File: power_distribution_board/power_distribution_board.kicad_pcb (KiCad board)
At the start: 2 copper layers, 67 parts, among them J1 CONN_01x03, J10 CONN_02X01, J11 CONN_02X01, J12 CONN_02X01, J13 CONN_02X01, J14 CONN_02X01, J15 CONN_02X01, J16 CONN_02X01, J17 CONN_02X01, J18 CONN_02X01, J19 CONN_02X01, J2 CONN_02X01, J20 CONN_02X01, J21 CONN_02X01, J22 CONN_02X01, J23 CONN_02X01, J3 CONN_02X01, J4 CONN_02X01, J5 CONN_02X01, J6 CONN_02X01, J7 CONN_02X01, J8 CONN_02X01, J9 CONN_02X01, Q1 NMOS_SSSGD, Q2 NMOS_SSSGD, Q3 NMOS_SSSGD, Q4 NMOS_SSSGD, Q5 Q_NMOS_GSD, U1 EHHD015A0A, U2 LTC1473, U3 EHHD010A0B, U4 LM317EMP, U5 BTS6133D, U6 A1120

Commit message: initial attempt at routing for LTC1743
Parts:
- moved J23 213.1 mm to (31.5, 116.5)
- moved J22 211.4 mm to (24.5, 116.5)
- moved D3 48.2 mm to (44.2, 131.2), turned to 180 degrees
- moved D5 37.2 mm to (44.2, 135.8), turned to 180 degrees
- moved Q3 33.4 mm to (62.8, 147.8), turned to 270 degrees
- moved R9 31.8 mm to (78.8, 138.0), turned to 180 degrees
- moved D6 25.4 mm to (46.0, 142.5), turned to 270 degrees
- moved Q2 22.7 mm to (71.0, 129.5), turned to 90 degrees
- moved Q4 21.5 mm to (69.2, 147.8), turned to 270 degrees
- moved Q1 17.4 mm to (64.5, 129.5), turned to 90 degrees
- moved C1 13.6 mm to (52.0, 140.0), turned to 270 degrees
- moved J1 13.6 mm to (57.8, 127.2), turned to 180 degrees
- moved C3 13.1 mm to (55.0, 140.0), turned to 270 degrees
- moved C2 12.3 mm to (53.5, 140.0), turned to 270 degrees
- moved R7 11.8 mm to (52.2, 137.0), turned to 180 degrees
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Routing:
- net Net-(R9-Pad2): track 0.00 -> 21.2 mm
- net Net-(R9-Pad3): track 0.00 -> 15.4 mm
- net Net-(Q2-Pad4): track 0.00 -> 13.7 mm
- net Net-(L1-Pad2): track 0.00 -> 12.6 mm
- net Net-(R5-Pad2): track 0.00 -> 8.75 mm
- net Net-(Q4-Pad4): track 0.00 -> 7.74 mm
- net Net-(Q3-Pad4): track 0.00 -> 6.91 mm
- net Net-(Q1-Pad4): track 0.00 -> 6.79 mm
- net Net-(C1-Pad1): track 0.00 -> 5.81 mm
- net Net-(J1-Pad1): track 0.00 -> 5.46 mm
- net Net-(J1-Pad3): track 0.00 -> 5.34 mm
- net Net-(J1-Pad2): track 0.00 -> 5.02 mm
- net Net-(R6-Pad2): track 0.00 -> 4.44 mm
- net Net-(C2-Pad1): track 0.00 -> 4.25 mm
- net Net-(R8-Pad2): track 0.00 -> 2.49 mm
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
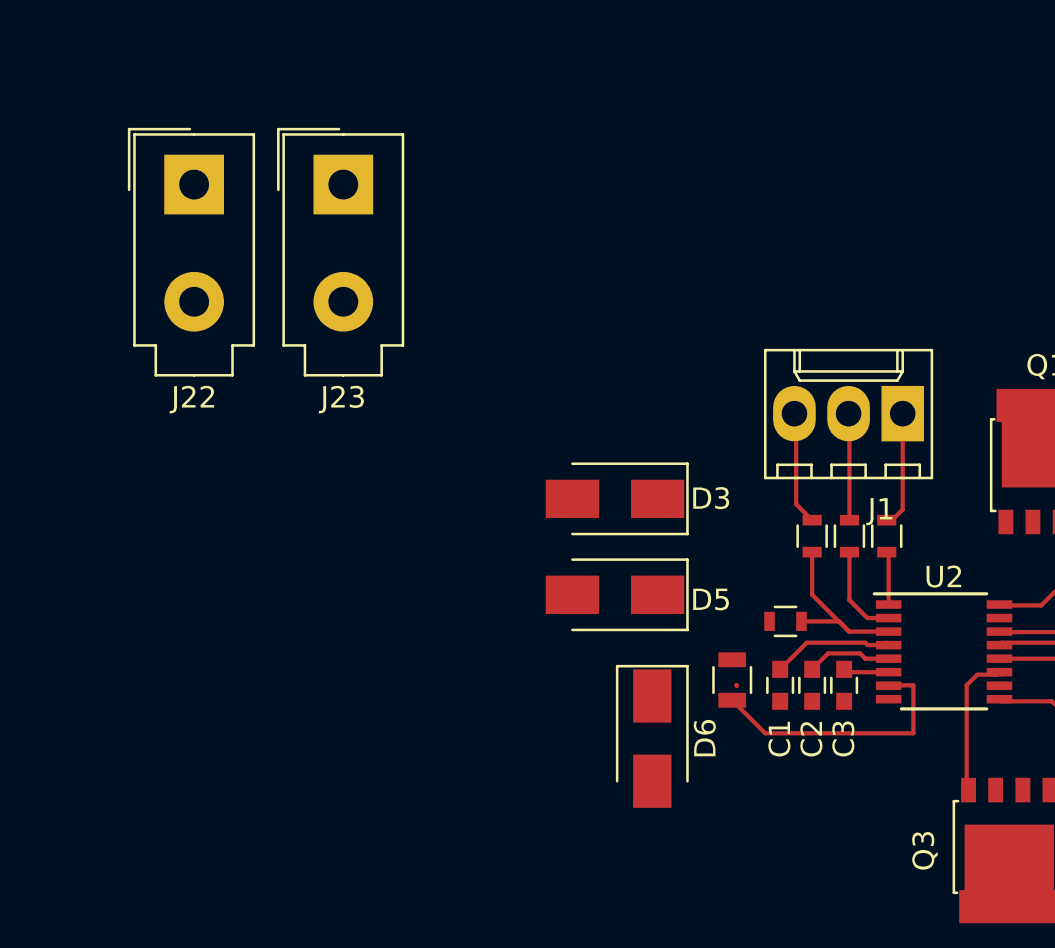
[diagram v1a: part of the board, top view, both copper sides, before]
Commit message: minor improvements to LTC1473 routing
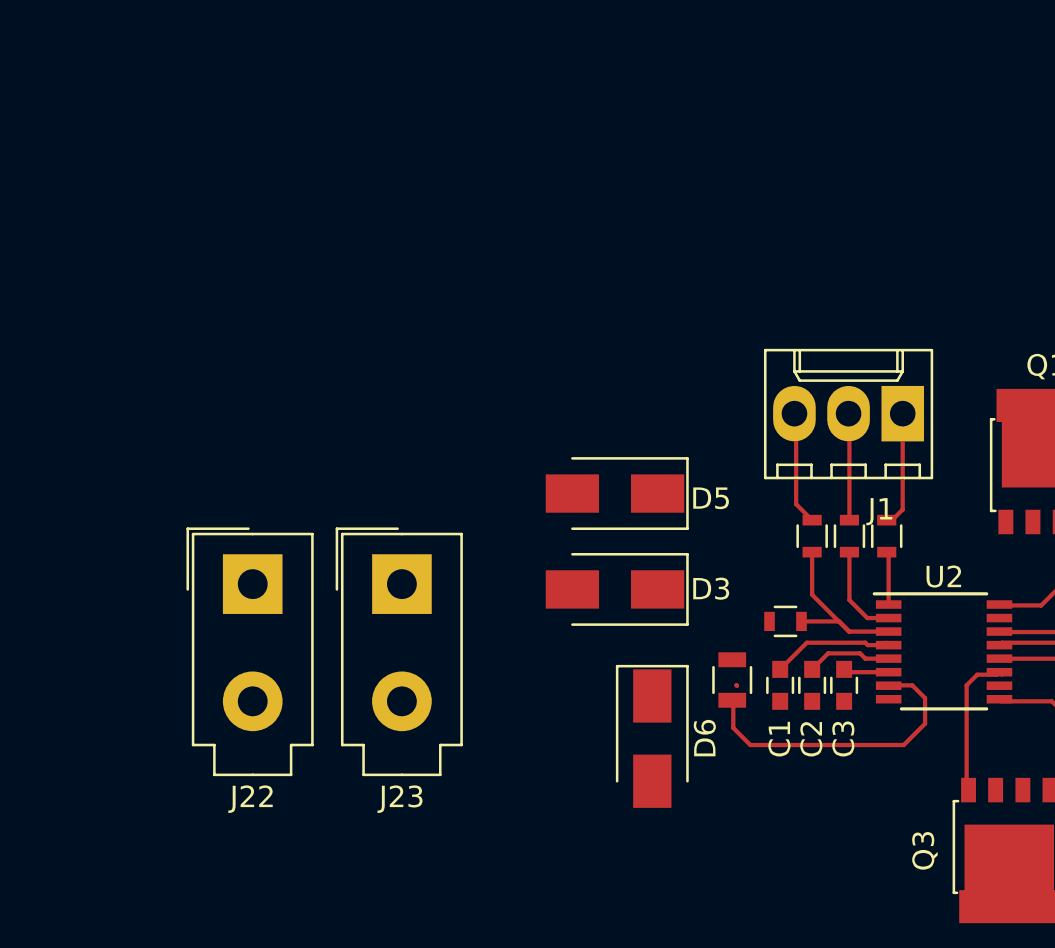
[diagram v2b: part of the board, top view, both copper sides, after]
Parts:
- moved J22 19.0 mm to (27.2, 135.2)
- moved J23 19.0 mm to (34.2, 135.2)
- moved D5 4.75 mm to (44.2, 131.0)
- moved D3 4.25 mm to (44.2, 135.5)
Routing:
- net Net-(L1-Pad2): track 12.6 -> 14.3 mm
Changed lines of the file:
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@@
     (thickness 1.6)
     (drawings 0)
-    (tracks 69)
+    (tracks 74)
     (zones 0)
     (modules 67)
@@
   )
   (module Diodes_SMD:D_SMA (layer F.Cu)
-    (at 44.25 131.25 180)
+    (at 44.25 135.5 180)
     (descr "Diode SMA (DO-214AC)")
     (tags "Diode SMA (DO-214AC)")
@@
   )
   (module Diodes_SMD:D_SMA (layer F.Cu)
-    (at 44.25 135.75 180)
+    (at 44.25 131 180)
     (descr "Diode SMA (DO-214AC)")
     (tags "Diode SMA (DO-214AC)")
@@
   )
   (module Connectors_Molex:Molex_MiniFit-JR-5556-02A_2x01x4.20mm_Straight (layer F.Cu)
-    (at 24.5 116.5)
+    (at 27.25 135.25)
     (descr "Molex Mini-Fit JR, PN:5556-02A, dual row, top entry type, through hole")
     (tags "connector molex mini-fit 5556")
@@
   )
   (module Connectors_Molex:Molex_MiniFit-JR-5556-02A_2x01x4.20mm_Straight (layer F.Cu)
-    (at 31.5 116.5)
+    (at 34.25 135.25)
     (descr "Molex Mini-Fit JR, PN:5556-02A, dual row, top entry type, through hole")
     (tags "connector molex mini-fit 5556")
@@
   (segment (start 52.75 131.5) (end 52.75 127.33) (width 0.2) (layer F.Cu) (net 15) (status 20))
   (segment (start 52.75 127.33) (end 52.67 127.25) (width 0.2) (layer F.Cu) (net 15) (status 30))
-  (segment (start 57.09 140.0175) (end 57.1075 140) (width 0.2) (layer F.Cu) (net 19))
-  (segment (start 57.1075 140) (end 58.25 140) (width 0.2) (layer F.Cu) (net 19))
-  (segment (start 58.25 140) (end 58.25 142.25) (width 0.2) (layer F.Cu) (net 19))
-  (segment (start 58.25 142.25) (end 51.3 142.25) (width 0.2) (layer F.Cu) (net 19))
-  (segment (start 51.3 142.25) (end 49.75 140.7) (width 0.2) (layer F.Cu) (net 19))
+  (segment (start 57.09 140.0175) (end 57.1075 140) (width 0.2) (layer F.Cu) (net 19) (status C00000))
+  (segment (start 57.1075 140) (end 58.2 140) (width 0.2) (layer F.Cu) (net 19) (status 400000))
+  (segment (start 49.8 142) (end 49.8 140.75) (width 0.2) (layer F.Cu) (net 19) (status 800000))
+  (segment (start 50.6 142.8) (end 49.8 142) (width 0.2) (layer F.Cu) (net 19))
+  (segment (start 57.8 142.8) (end 50.6 142.8) (width 0.2) (layer F.Cu) (net 19))
+  (segment (start 58.8 141.8) (end 57.8 142.8) (width 0.2) (layer F.Cu) (net 19))
+  (segment (start 58.8 140.6) (end 58.8 141.8) (width 0.2) (layer F.Cu) (net 19))
+  (segment (start 58.2 140) (end 58.8 140.6) (width 0.2) (layer F.Cu) (net 19))
+  (segment (start 49.8 140.75) (end 49.75 140.7) (width 0.2) (layer F.Cu) (net 19) (status C00000))
+  (segment (start 49.8 140.75) (end 49.75 140.7) (width 0.2) (layer F.Cu) (net 19) (status C00000))
   (segment (start 66.41 132.335) (end 66.25 132.495) (width 0.2) (layer F.Cu) (net 21) (status 30))
   (segment (start 66.25 132.495) (end 66.25 134.25) (width 0.2) (layer F.Cu) (net 21) (status 10))

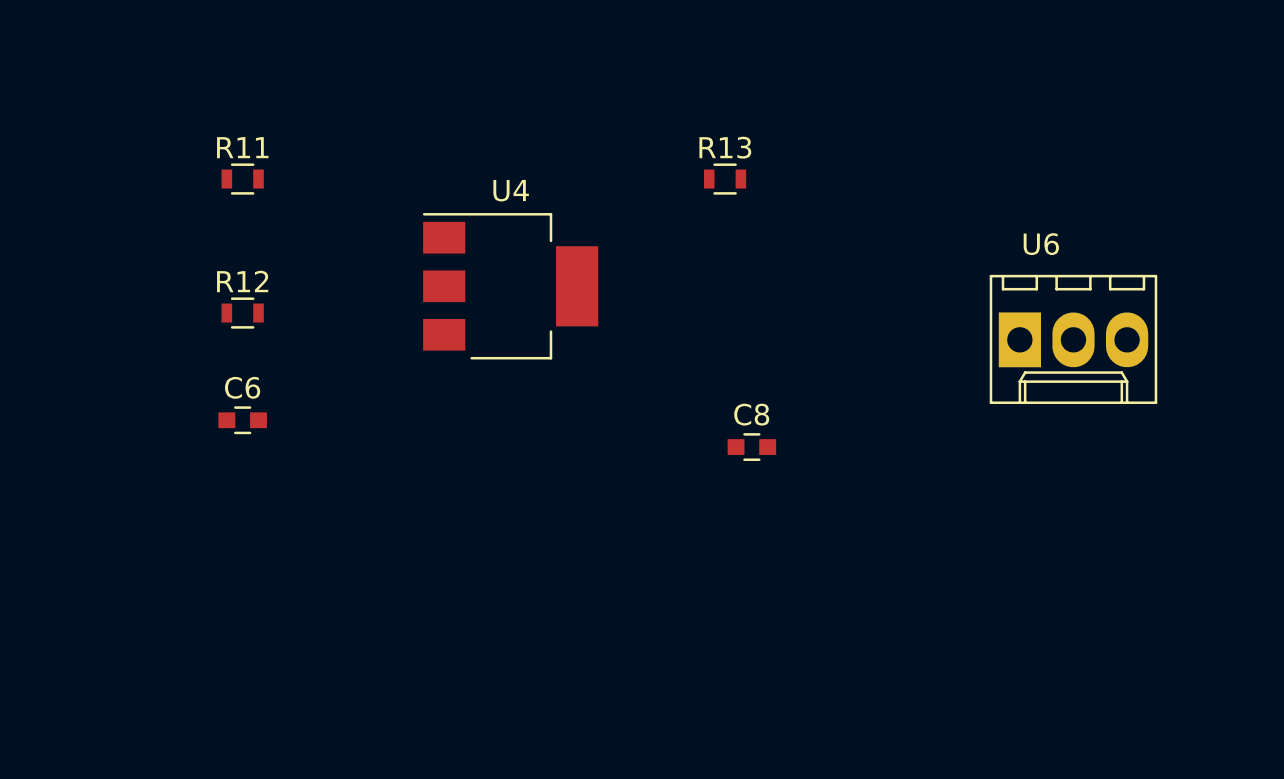
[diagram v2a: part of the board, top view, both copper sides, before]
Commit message: initial routing of killswitch subcircuit
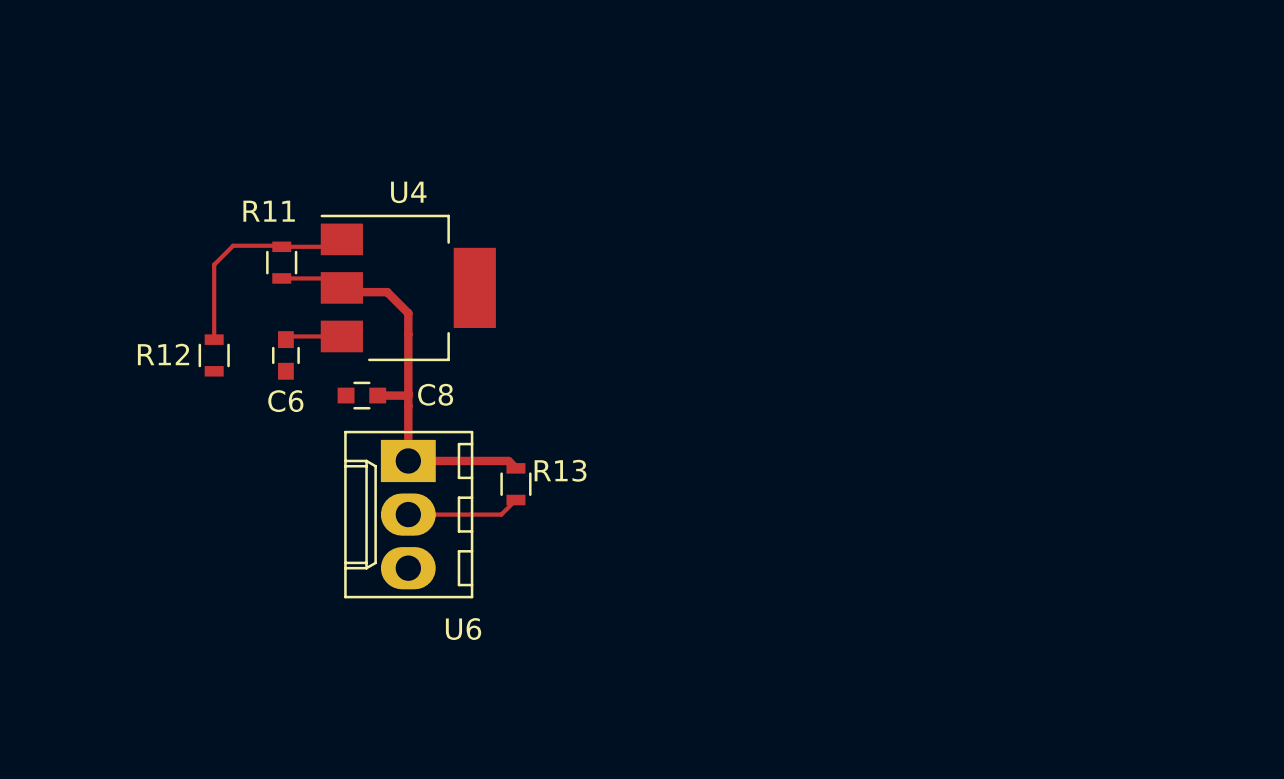
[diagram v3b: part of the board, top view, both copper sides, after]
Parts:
- moved U6 29.5 mm to (166.6, 130.2), turned to 270 degrees
- moved C8 18.6 mm to (164.4, 127.1)
- moved R13 17.5 mm to (171.7, 131.3), turned to 90 degrees
- moved U4 4.85 mm to (166.6, 122.0)
- moved R11 4.37 mm to (160.6, 120.8), turned to 90 degrees
- moved C6 3.69 mm to (160.8, 125.2), turned to 90 degrees
- moved R12 2.42 mm to (157.4, 125.2), turned to 270 degrees
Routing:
- net /AO_PWR: track 0.00 -> 20.5 mm
- net Net-(R11-Pad2): track 0.00 -> 10.1 mm
- net /PWR_ENABLE: track 0.00 -> 5.39 mm
- net /PWR_SWITCHED: track 0.00 -> 2.71 mm
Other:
- net class 0.4mm added: clearance 0.2, trace_width 0.4, via_dia 0.6, via_drill 0.4
